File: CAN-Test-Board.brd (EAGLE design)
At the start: 54.6 x 70.8 mm, 47 parts, among them Y1 ECS-80-S-4X, Y2 ECS-80-S-4X

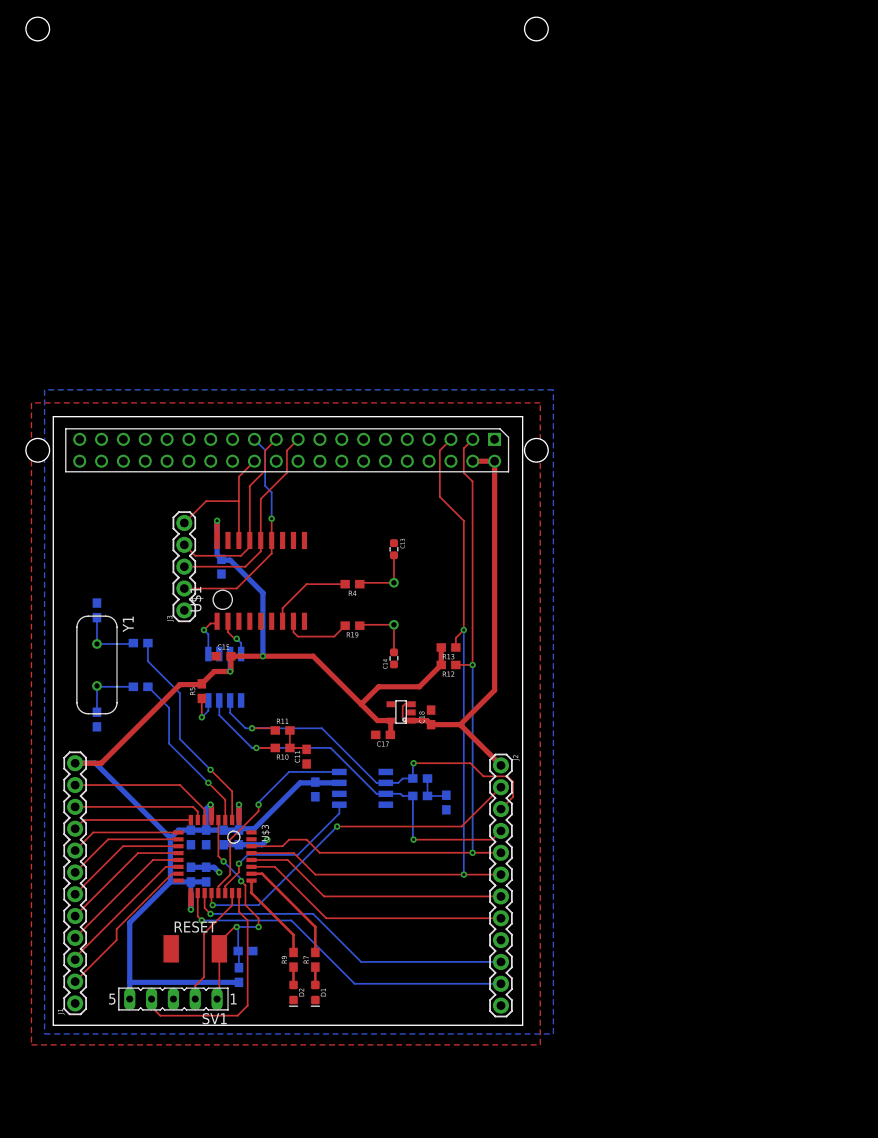
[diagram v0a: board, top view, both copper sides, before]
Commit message: smaller and extra CAN breakouts
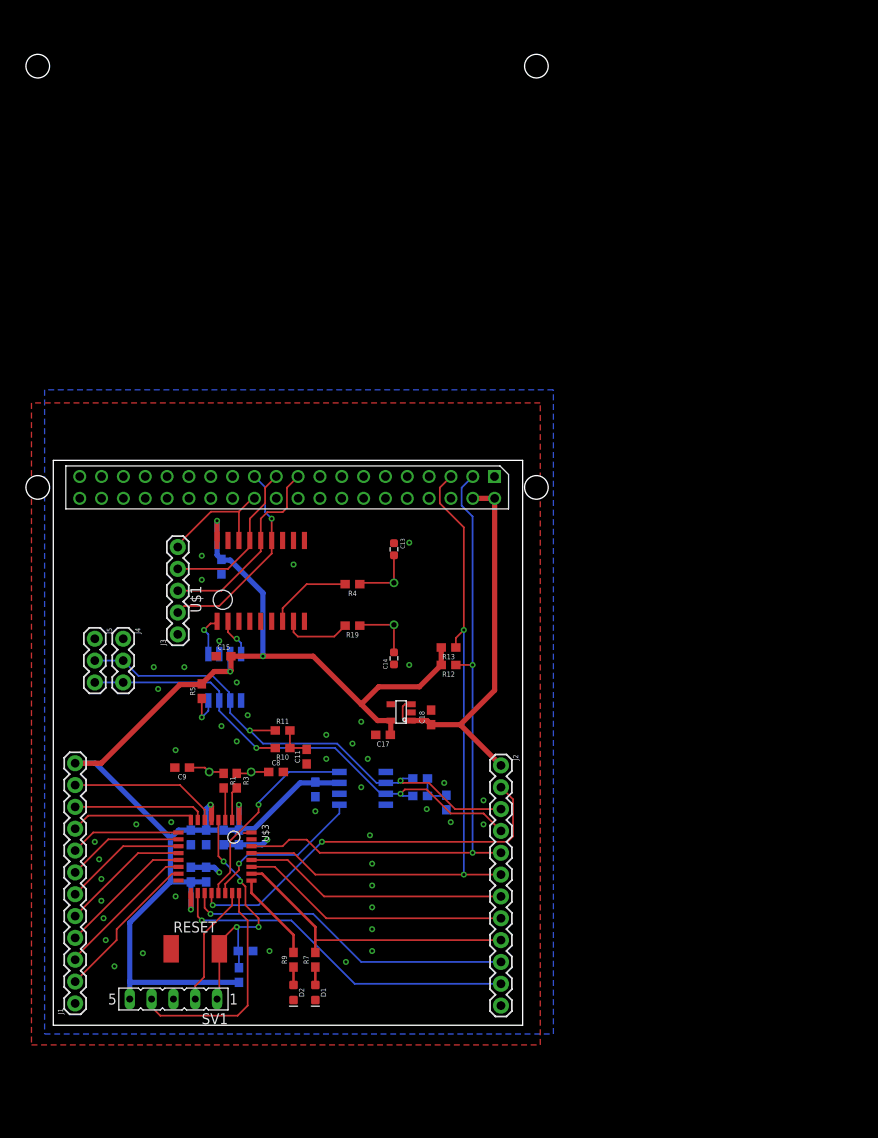
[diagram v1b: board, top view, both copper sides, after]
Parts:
- added J4, J5: (no value), SparkFun-Connectors:1X03
- moved C8 28.1 mm to (25.9, 29.5), flipped to the top, turned to 0 degrees
- moved Y1 19.9 mm to (20.6, 29.5), flipped to the bottom, turned to 0 degrees
- moved R3 19.5 mm to (21.3, 28.4), flipped to the top, turned to 270 degrees
- moved R1 14.6 mm to (19.8, 28.4), flipped to the top, turned to 270 degrees
- moved C9 11.4 mm to (15.0, 30.0), flipped to the top, turned to 180 degrees
- moved PCB1 4.32 mm to (59.7, 115.1)
- moved J3 2.90 mm to (14.5, 45.5)
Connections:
- removed net PB3: J2.9
- net CAN_H: now also J4.3, J5.3
- net CAN_L: now also J4.2, J5.2
- net GND: now also J4.1, J5.1
- net LED2: now also J2.9
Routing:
- net LED2: track 13.0 -> 34.5 mm
- net OSC_IN: track 24.6 -> 3.94 mm, vias 1 -> 0
- net OSC_OUT: track 19.2 -> 3.80 mm, vias 1 -> 0
- net CAN_H: track 46.0 -> 59.9 mm
- net CAN_L: track 47.1 -> 60.4 mm
- net PA10: track 40.7 -> 46.0 mm
- net SCL: track 84.8 -> 80.5 mm
- net 5V: track 51.1 -> 46.8 mm
- net SDA: track 80.8 -> 76.7 mm
- net N$2: track 7.33 -> 3.79 mm
- net MISO: track 22.4 -> 18.9 mm
- net N$1: track 7.29 -> 4.26 mm
- net CS: track 17.4 -> 14.8 mm
- net SCLK: track 26.0 -> 23.6 mm
- net MOSI: track 24.5 -> 23.1 mm
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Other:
- board size 54.6 x 70.8 mm -> 54.6 x 65.7 mm

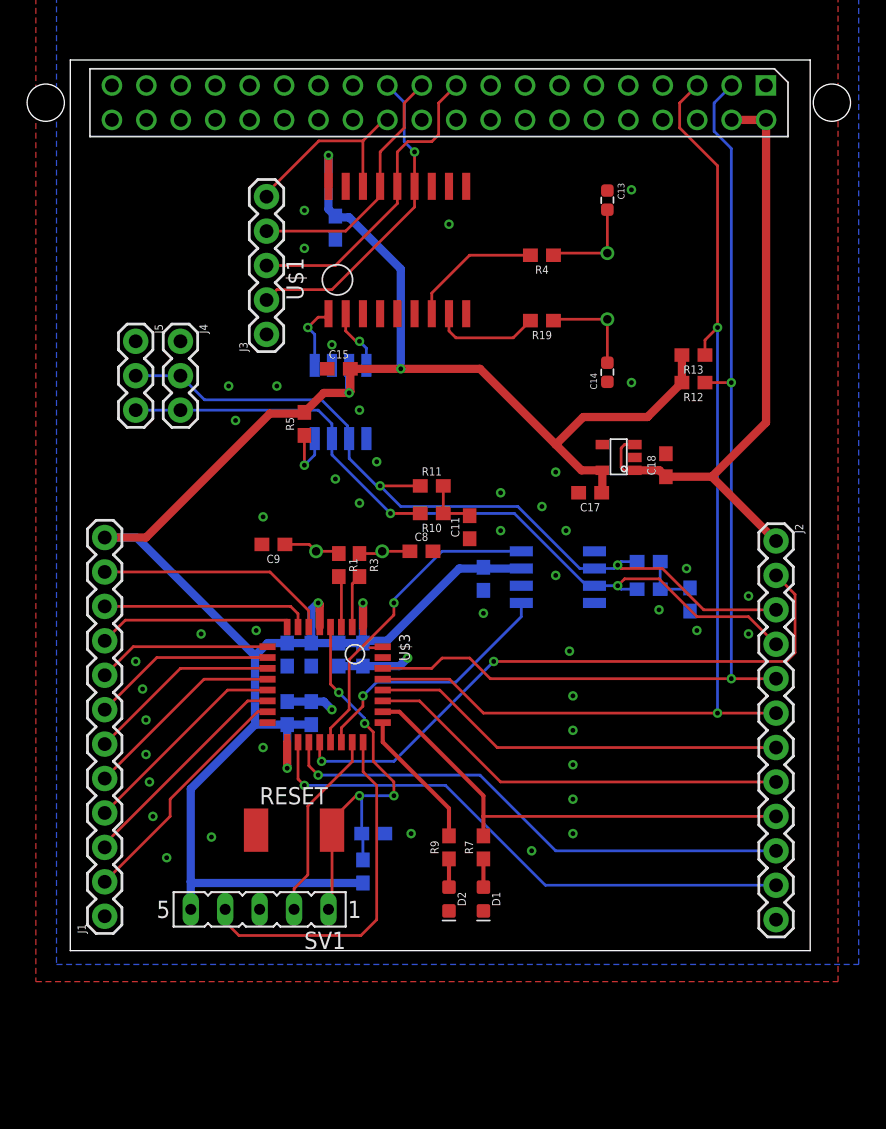
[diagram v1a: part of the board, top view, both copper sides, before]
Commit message: labels and 3v3 power options
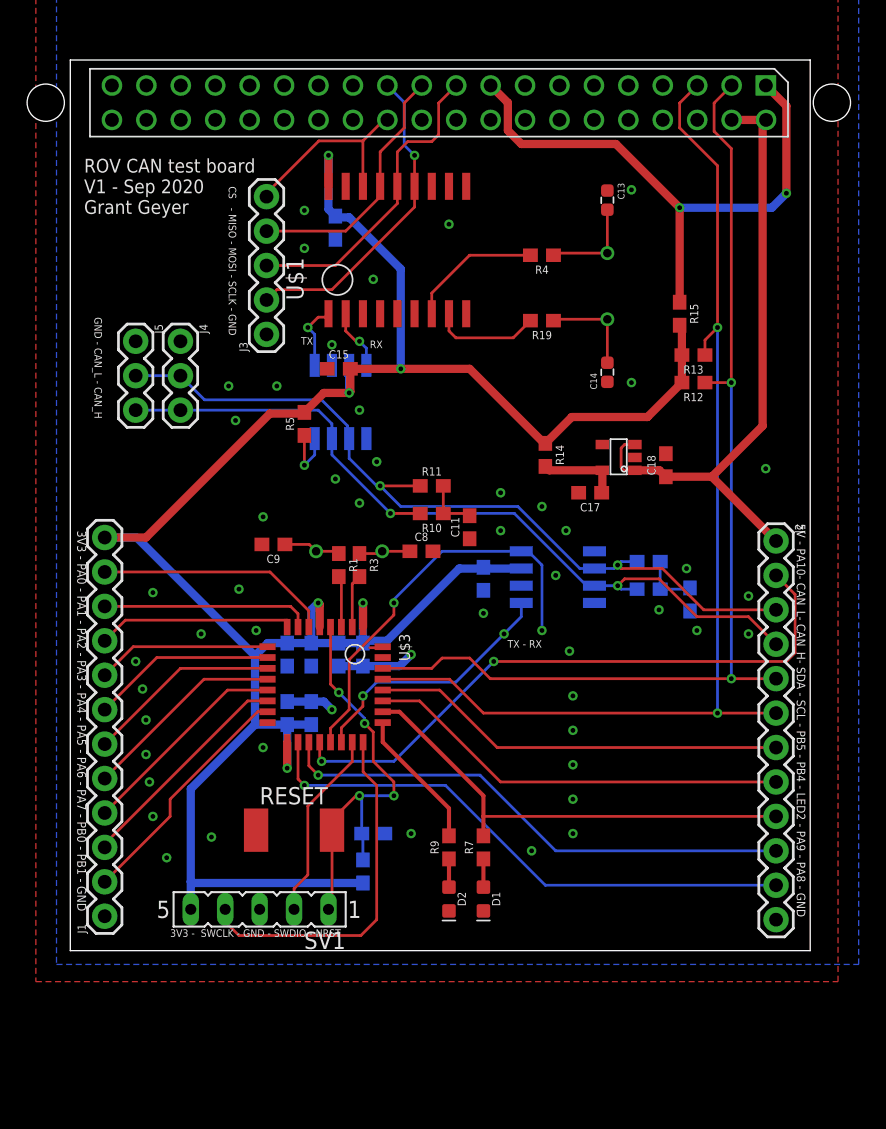
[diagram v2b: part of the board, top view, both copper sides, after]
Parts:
- added R14: (no value), SparkFun-Resistors:0603
- added R15: 0, SparkFun-Resistors:0603
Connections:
- new net 3V3_PI: PCB1.P$1, PCB1.P$17, R15.1
- new net 3V3_REG: C17.1, R14.2, U$5.P$5
- net 3V3: now also R14.1, R15.2; no longer C17.1, U$5.P$5
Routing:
- net 3V3_PI: track 0.00 -> 42.7 mm, vias 0 -> 2
- net CAN_RX_STM: track 23.3 -> 30.1 mm, vias 1 -> 2
- net 3V3_REG: track 0.00 -> 6.00 mm
- net 3V3: track 173.3 -> 169.5 mm
- net GND: track 9.86 -> 10.2 mm, vias 47 -> 50
- net CAN_TX_STM: vias 1 -> 2
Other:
- board text added: "3V3 - PA0 - PA1 - PA2 - PA3 - PA4 - PA5 - PA6 - PA7 - PB0 - PB1 - GND"
- board text added: "3V3 - SWCLK - GND - SWDIO - NRST"
- board text added: "5V - PA10- CAN_L- CAN_H- SDA - SCL - PB5 - PB4 - LED2 - PA9 - PA8 - GND"
- board text added: "CS - MISO - MOSI - SCLK - GND"
- board text added: "GND - CAN_L - CAN_H"
- board text added: "ROV CAN test board V1 - Sep 2020 Grant Geyer"
- board text added: "RX"
- board text added: "TX"
- board text added: "TX - RX"

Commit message: smaller
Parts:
- moved C13 9.51 mm to (34.3, 47.5)
- moved Y2 8.69 mm to (34.3, 42.2)
- moved C14 8.10 mm to (34.3, 36.6)
- moved R19 7.97 mm to (30.7, 39.6)
- moved R4 7.97 mm to (30.7, 44.5)
- moved J3 6.35 mm to (9.40, 41.7)
- moved C15 6.02 mm to (22.6, 37.6), flipped to the bottom, turned to 90 degrees
- moved PCB1 5.93 mm to (58.7, 109.2)
- moved J4 5.80 mm to (5.33, 39.9)
- moved J5 5.80 mm to (2.03, 39.9)
- moved R13 5.71 mm to (43.9, 38.6)
- moved R12 5.47 mm to (43.9, 36.8)
- moved R15 5.43 mm to (43.9, 41.7)
- moved U$1 4.99 mm to (27.9, 42.2)
- moved C16 4.33 mm to (42.4, 23.1)
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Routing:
- net SCL: track 80.5 -> 71.8 mm
- net 5V: track 46.8 -> 39.1 mm
- net SDA: track 76.7 -> 70.0 mm
- net 3V3_PI: track 42.7 -> 37.6 mm, vias 2 -> 0
- net CAN_RX_PI: track 4.59 -> 9.67 mm, vias 1 -> 2
- net OSC2: track 9.96 -> 5.88 mm
- net PA10: track 46.0 -> 42.0 mm
- net OSC1: track 8.01 -> 5.51 mm
- net MISO: track 18.9 -> 21.4 mm
- net N$3: track 7.24 -> 4.96 mm
- net MOSI: track 23.1 -> 25.3 mm
- net 3V3: track 169.5 -> 167.5 mm, vias 6 -> 5
- net N$4: track 7.22 -> 5.19 mm
- net 3V3_REG: track 6.00 -> 4.13 mm
- net SCLK: track 23.6 -> 25.4 mm
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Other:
- board size 54.6 x 65.7 mm -> 52.3 x 59.4 mm

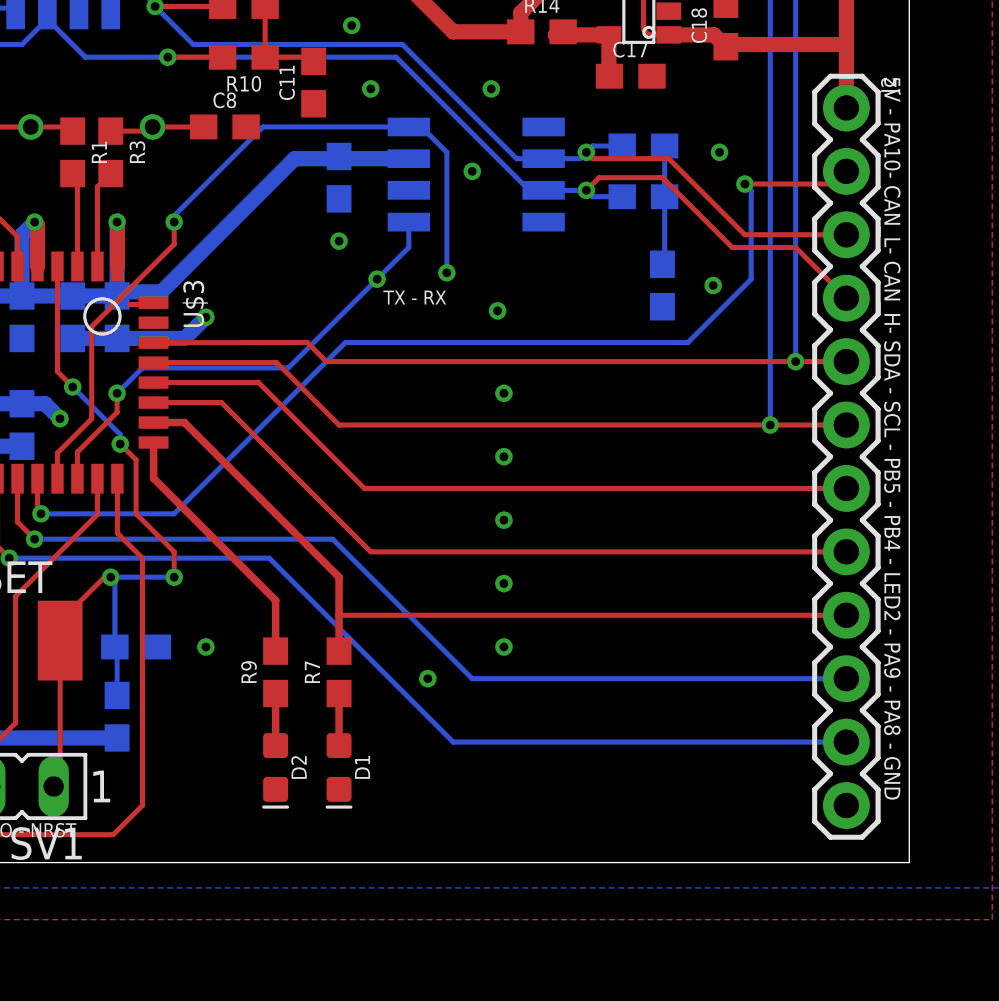
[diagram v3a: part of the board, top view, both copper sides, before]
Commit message: added samtec t2i
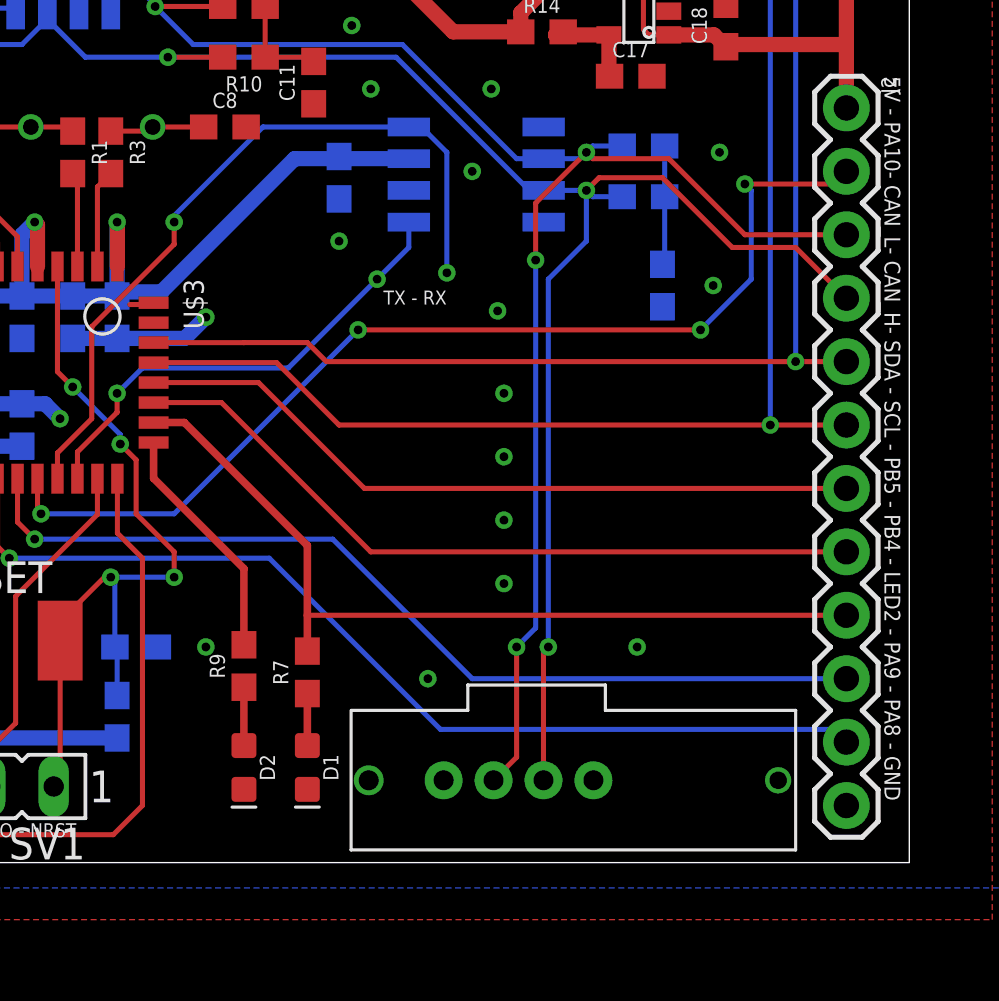
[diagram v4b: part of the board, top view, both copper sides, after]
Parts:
- added U$4: T2I, Samtec t2i:T2I
- moved R9 1.30 mm to (25.7, 7.87)
- moved D1 1.27 mm to (28.2, 3.81)
- moved D2 1.27 mm to (25.7, 3.81)
- moved R7 1.27 mm to (28.2, 7.62)
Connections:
- net CAN_H: now also U$4.2
- net CAN_L: now also U$4.3
- net GND: now also U$4.1, U$4.4
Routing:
- net CAN_L: track 58.8 -> 85.5 mm, vias 2 -> 4
- net CAN_H: track 59.7 -> 84.1 mm, vias 2 -> 3
- net LED1: track 10.4 -> 9.60 mm
- net LED2: track 33.3 -> 34.0 mm
- net PA10: vias 2 -> 4
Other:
- board text added: "CAN_H - CAN_L"
